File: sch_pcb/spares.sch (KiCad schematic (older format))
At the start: 75 parts, among them J305 AUX_IO_1, J307 SPARE, J308 AUX_IO_2, J311 I2C1_5V, J312 RTC, J315 OLED_SSD1306, P301 Chassis, U106 MCP6004T, U108 74LVC4066, U301 MCP23017, U304 MCP3008, U305 MCP1703A-2502/MB, U306 TPS54302, U307 IP4234CZ6, U308 IP4234CZ6

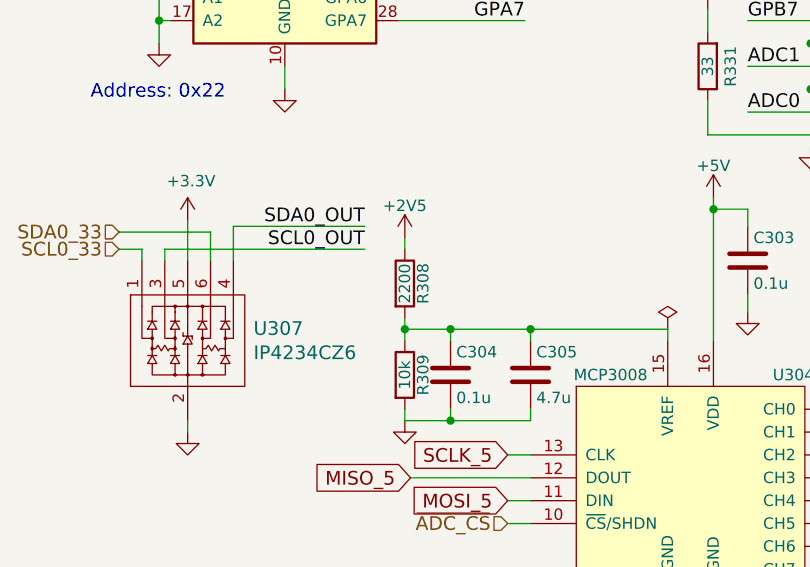
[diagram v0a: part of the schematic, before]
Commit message: Change 33pf to 100pf.  Change 2k and 2200 to 2k2.  Change I2C addresses for MCP23008.  Nudge link connectors
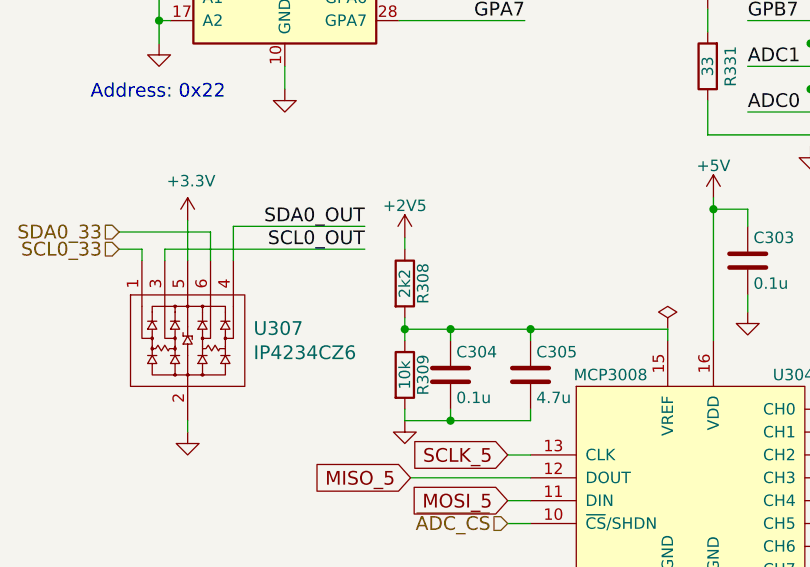
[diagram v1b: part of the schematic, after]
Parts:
- R308: value 2200 -> 2k2
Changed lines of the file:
@@
 P 4925 3875
 F 0 "R308" V 5005 3875 50  0000 C CNN
-F 1 "2200" V 4925 3875 50  0000 C CNN
+F 1 "2k2" V 4925 3875 50  0000 C CNN
 F 2 "lib:smd0603" V 4855 3875 50  0001 C CNN
 F 3 "" H 4925 3875 50  0001 C CNN

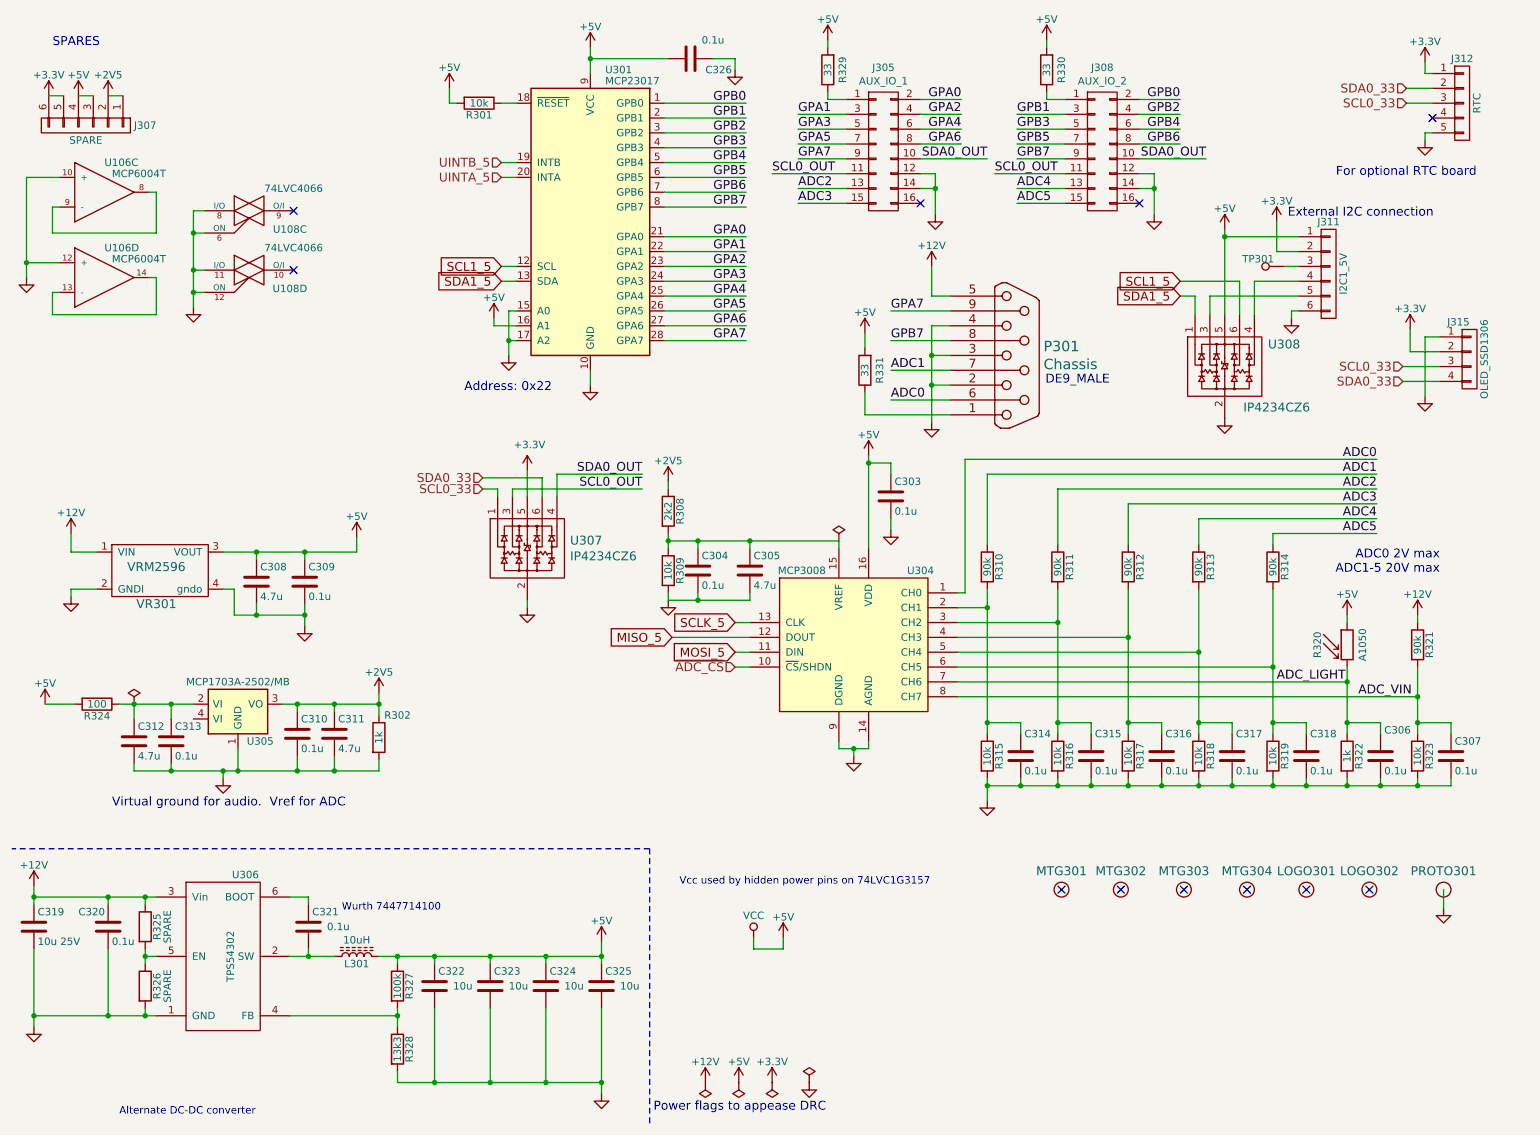
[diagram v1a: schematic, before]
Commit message: Add files via upload
Fix i2c addressing
Change footprint for LDR
Move connectors for temp/hum sensor and rtc so they won't hit the Pi
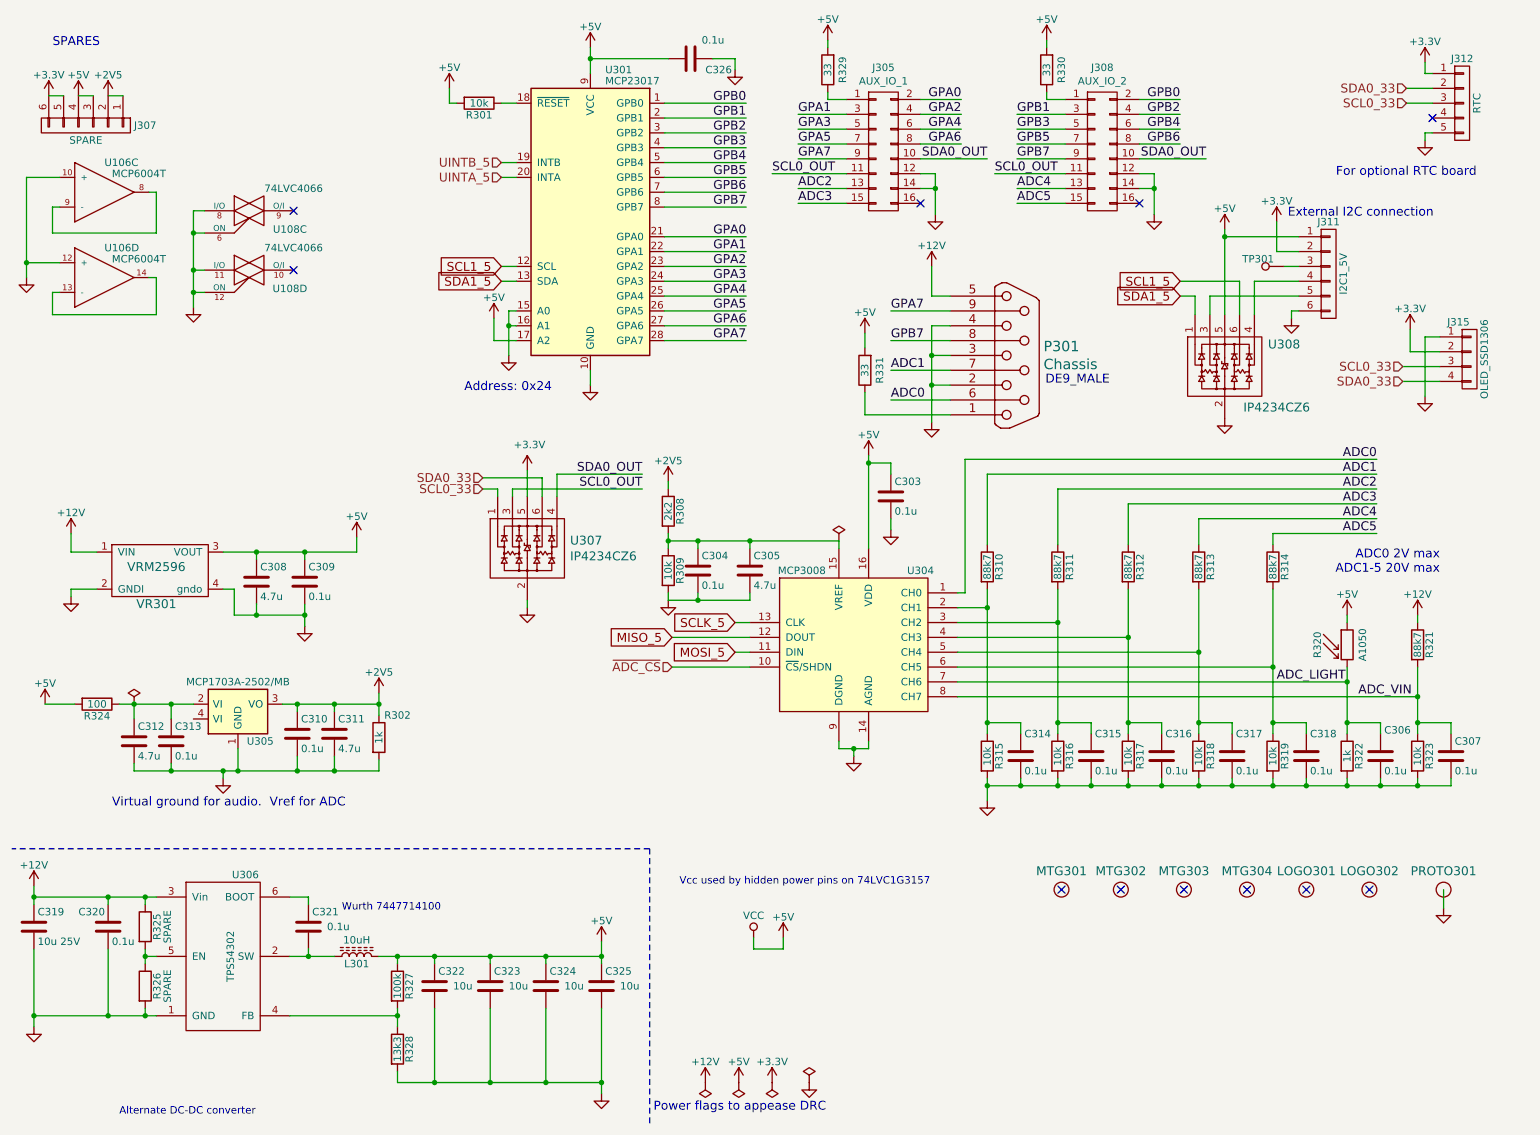
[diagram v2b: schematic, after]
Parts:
- R310, R311, R312, R313, R314, R321: value 90k -> 88k7
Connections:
- net +5V: now also U301.17 (A2); no longer U301.16 (A1)
- net GND: now also U301.16 (A1); no longer U301.17 (A2)
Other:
- note added: "Address: 0x24"
- note removed: "Address: 0x22"

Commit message: Add Digikey part # to all parts.  Fix unconnected nets
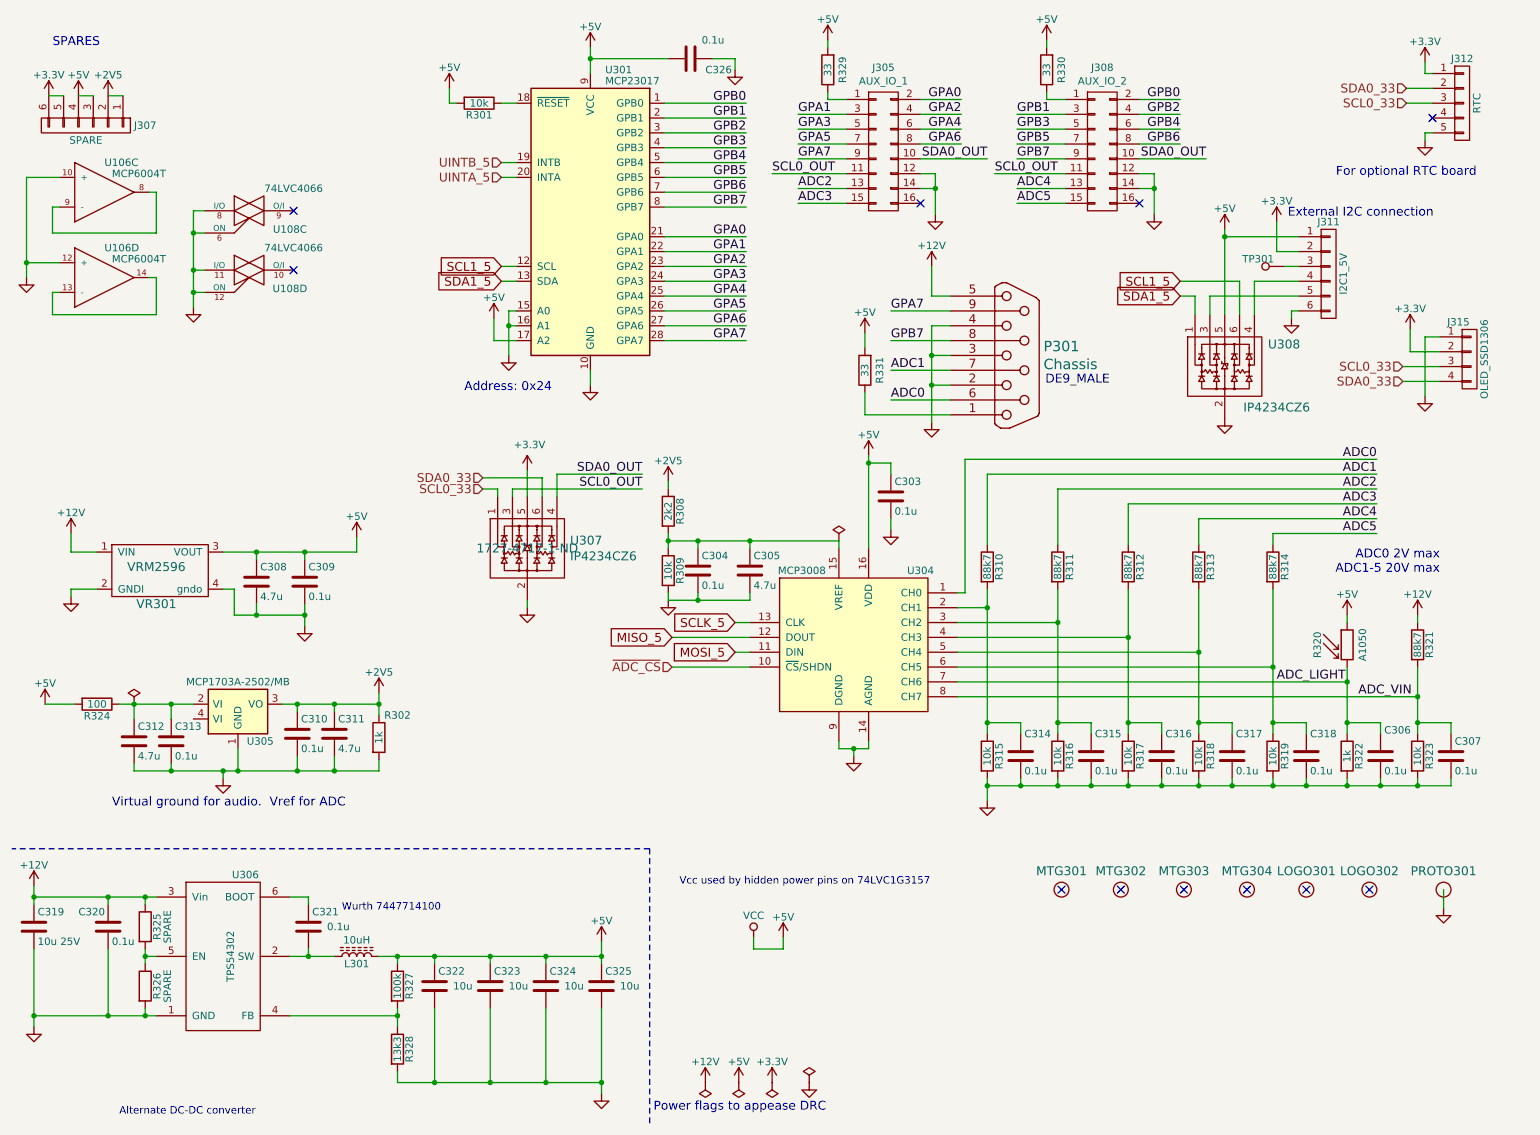
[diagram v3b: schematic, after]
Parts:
- C303, C304, C306, C307, C309, C310, C313, C314, C315, C316, C317, C318, C320, C321, C326: Digikey PN (none) -> 399-1096-1-ND
- C305, C308, C311, C312: Digikey PN (none) -> 1276-2087-1-ND
- C319: Digikey PN (none) -> 478-7436-1-ND
- C322, C323, C324, C325: Digikey PN (none) -> 478-5165-1-ND
- J305, J308: Digikey PN (none) -> ED10523-ND
- J311: Digikey PN (none) -> S1012EC-06-ND
- L301: Digikey PN (none) -> 732-2988-1-ND
- P301: Digikey PN (none) -> 609-5183-ND
- R301, R309, R315, R316, R317, R318, R319, R323: Digikey PN (none) -> 311-10KGRCT-ND
- R302, R322: Digikey PN (none) -> 311-1.0KGRCT-ND
- R308: Digikey PN (none) -> 311-2.2KGRCT-ND
- R310, R311, R312, R313, R314, R321: Digikey PN (none) -> 311-88.7KHRCT-ND
- R320: footprint lib:smd0603 -> lib:LDR
- R324: Digikey PN (none) -> 311-100GRCT-ND
- R327: Digikey PN (none) -> 311-100KGRCT-ND
- R328: Digikey PN (none) -> 311-13.3KHRCT-ND
- R329, R330, R331: Digikey PN (none) -> 311-33GRCT-ND
- U106: Digikey PN (none) -> MCP6004-I/SL-ND
- U108: Digikey PN (none) -> 1727-6368-1-ND
- U301: Digikey PN (none) -> MCP23017-E/SO-ND
- U304: Digikey PN (none) -> MCP3008-I/SL-ND
- U305: Digikey PN (none) -> MCP1700T-2502E/MBCT-ND
- U306: Digikey PN (none) -> 296-46237-1-ND
- U307, U308: Digikey PN (none) -> 1727-4717-1-ND

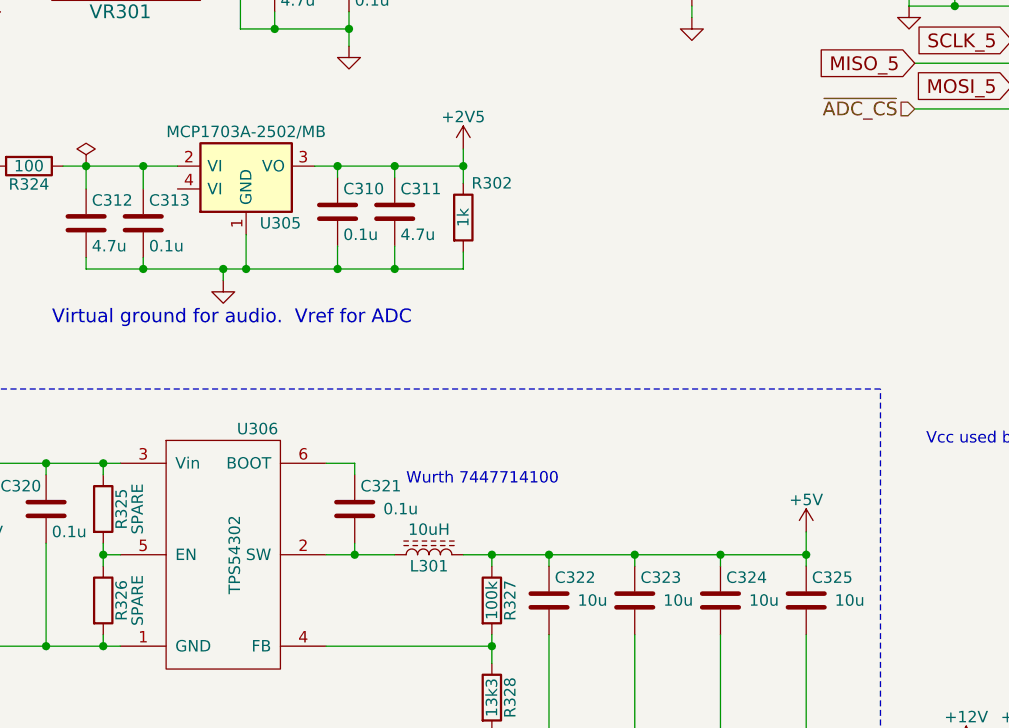
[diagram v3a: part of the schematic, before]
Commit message: Switch to 0402 parts and SeeedStudio footprints
Silk screen is still being updated.  BOM needs to be updated as well
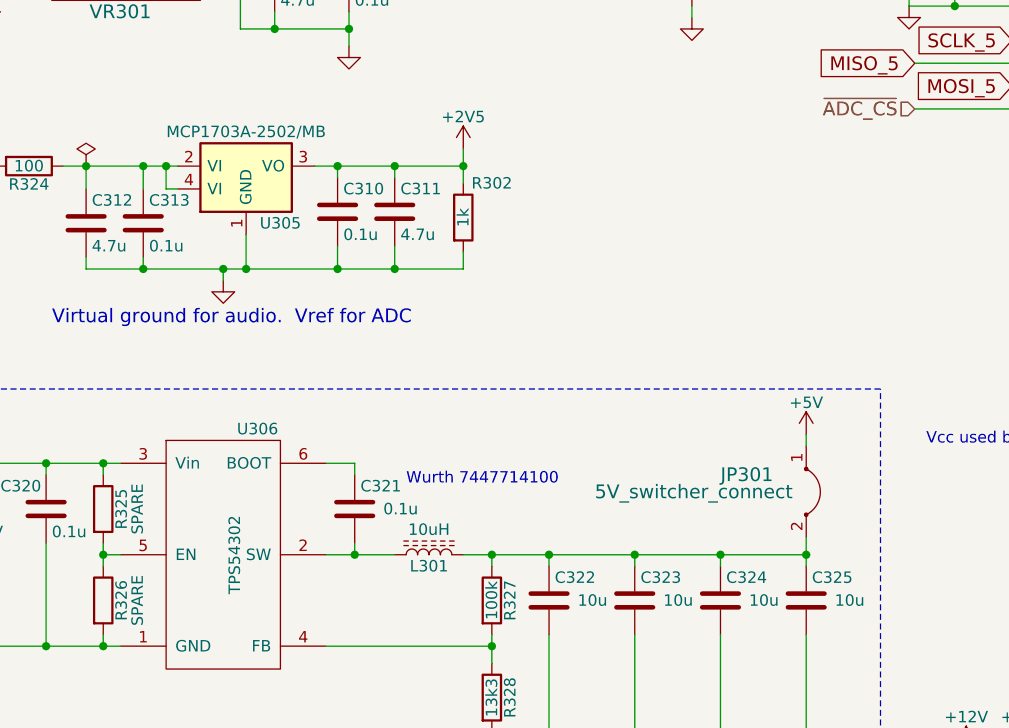
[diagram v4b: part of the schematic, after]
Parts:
- added JP301: 5V_switcher_connect, lib:JUMPER_2PIN_CUTTABLE, symbol 2_pin_cuttable_jumper
- C303, C304, C305, C306, C307, C308, C309, C310, C311, C312, C313, C314, C315, C316, C317, C318, C320, C321, C326: footprint lib:smd0603 -> lib:OPL_C0402
- C319: footprint lib:smd1210 -> lib:OPL_C0805
- C322, C323, C324, C325: footprint lib:smd0805 -> lib:OPL_C0805
- J307, J311: footprint lib:SIL-6 -> lib:OPL_H6-2.54
- J315: footprint lib:SIL-4 -> lib:OPL_H4-2.54
- R301, R302, R308, R309, R310, R311, R312, R313, R314, R315, R316, R317, R318, R319, R321, R322, R323, R324, R325, R326, R327, R328, R329, R330, R331: footprint lib:smd0603 -> lib:OPL_R0402
- U305: footprint lib:sot89 -> lib:OPL_SOT-89
- U306, U307, U308: footprint lib:SOT23-6 -> lib:OPL_SOT-23-6
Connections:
- net +5V: now also JP301.1; no longer C322.1, C323.1, C324.1, C325.1, L301.1, R327.1
- net at C312.1, C313.1, R324.1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: now also U305.4 (VI)
- new net: C322.1, C323.1, C324.1, C325.1, JP301.2, L301.1, R327.1
